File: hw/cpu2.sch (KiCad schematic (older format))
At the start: 0 parts

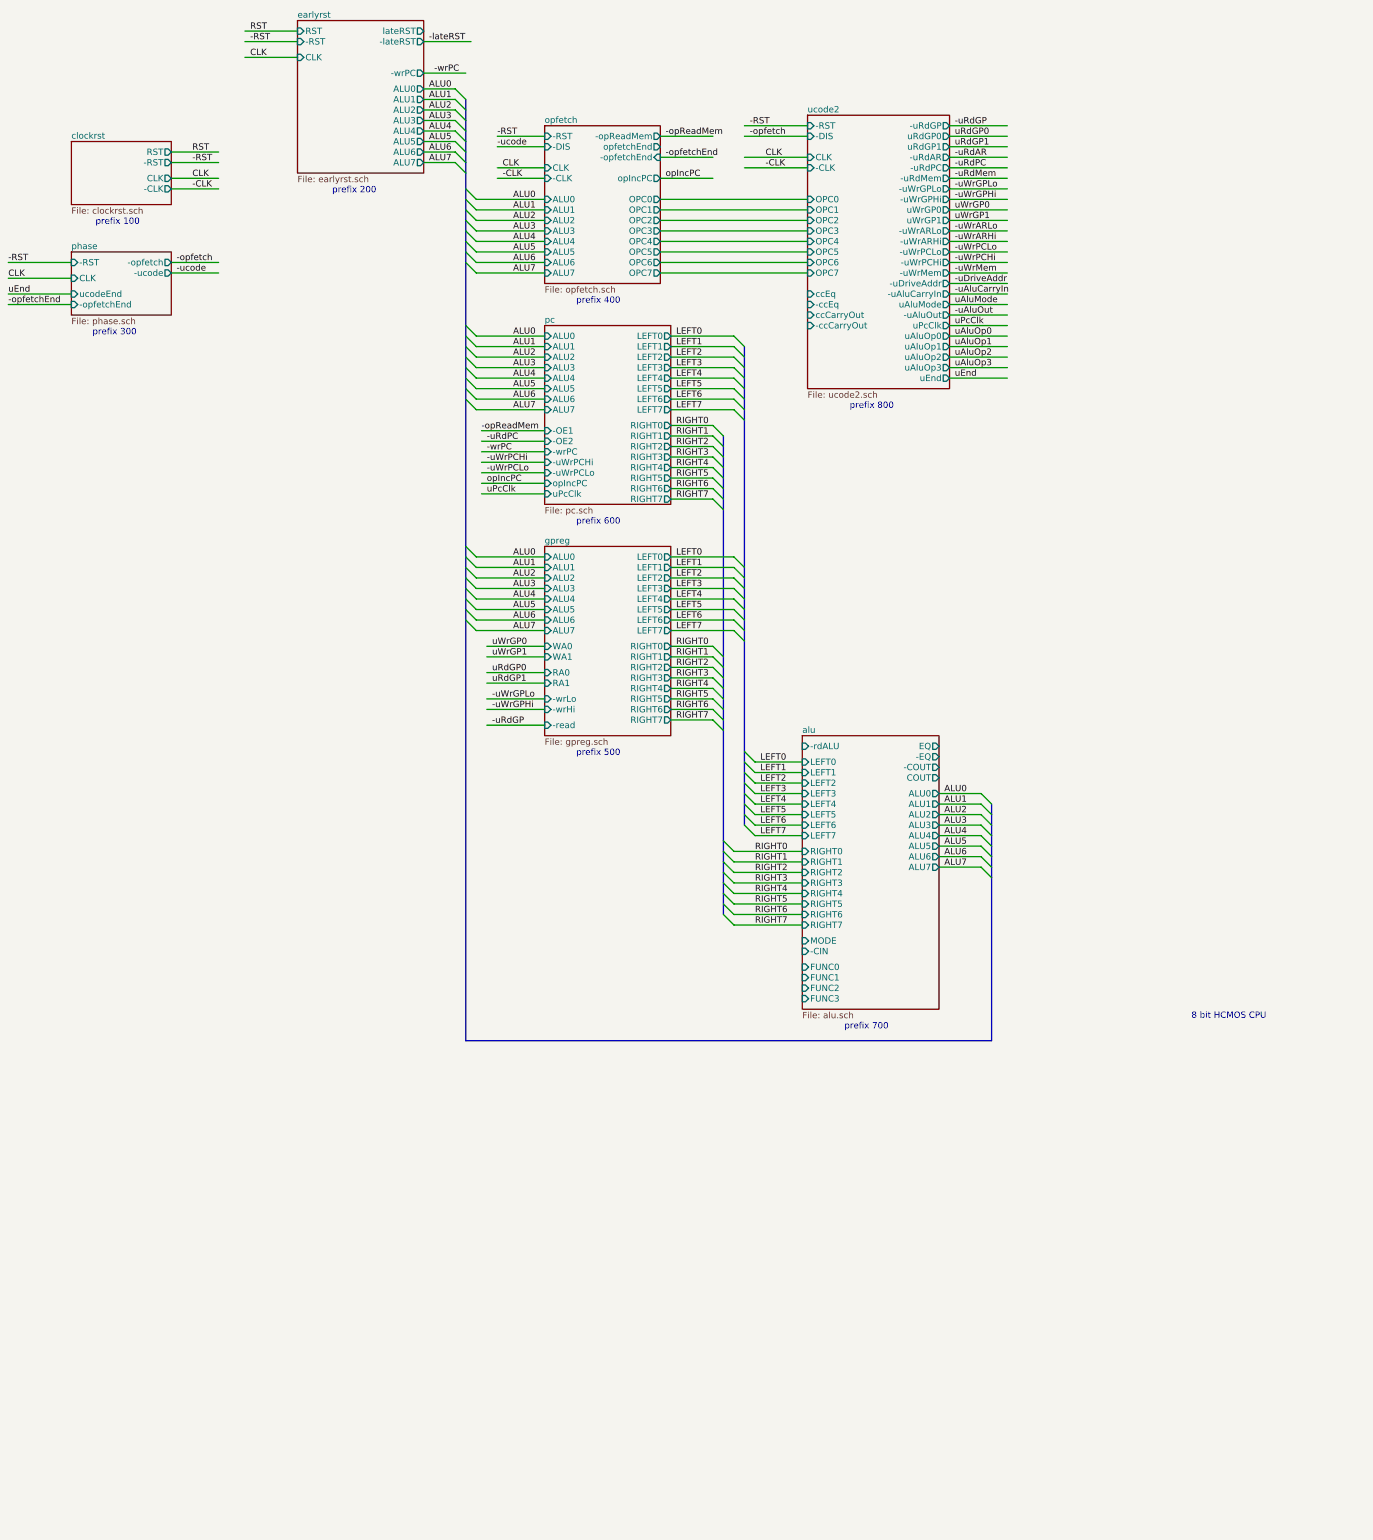
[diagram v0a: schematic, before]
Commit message: added bus/address register module
Used a '245 bus transceiver to do reads from
and writes to the external data bus, so the
control signals for reading and writing memory
changed (to -rwMem and memDir, rather than
separate read and write signals.)

At this point, I think all of the required modules
are in place, although not all of the connections are
shown on the top-level schematic.
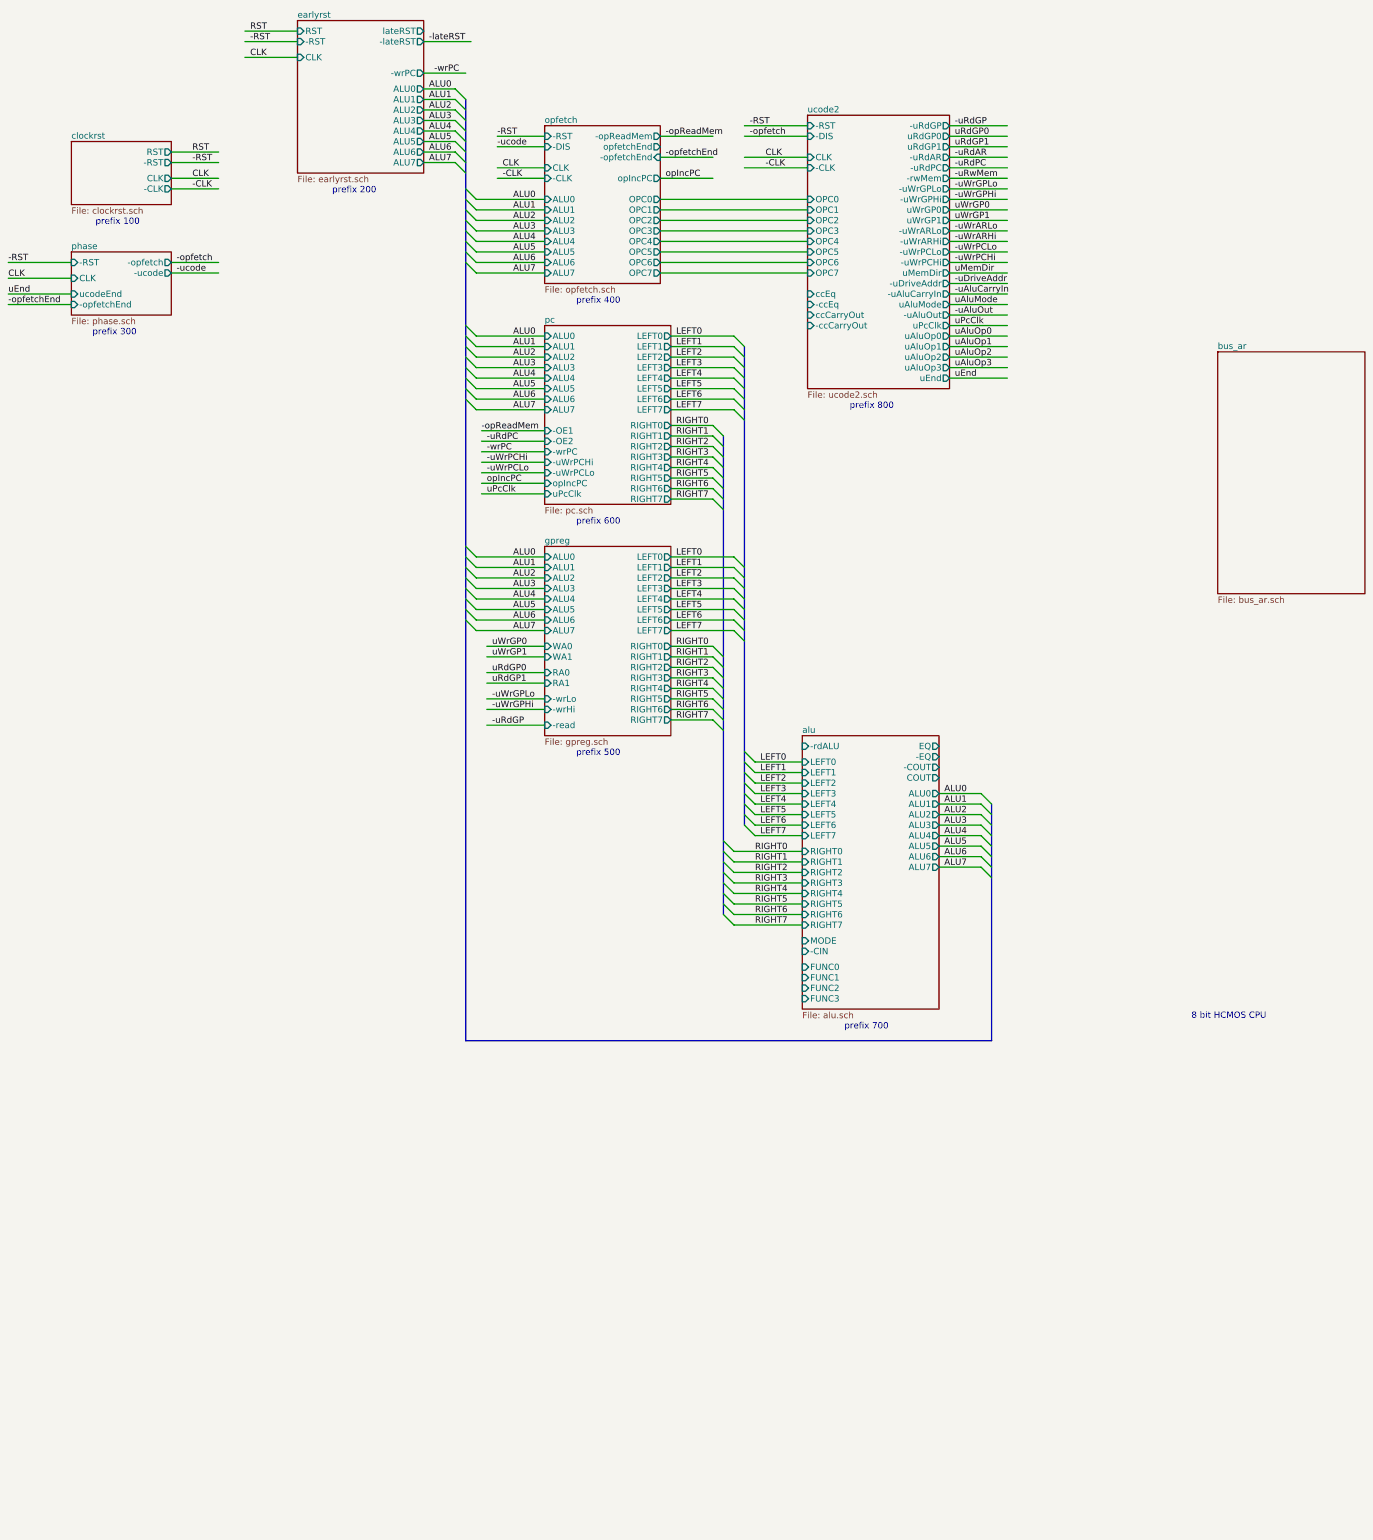
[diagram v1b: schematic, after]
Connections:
- net labels added: -uRwMem, uMemDir
- net labels removed: -uRdMem, -uWrMem
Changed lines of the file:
@@
 $Descr A3 16535 11693
 encoding utf-8
-Sheet 1 9
+Sheet 1 10
 Title ""
 Date ""
@@
 	4700 2050 5000 2050
 Wire Bus Line
-	5100 1450 5100 1550
-Wire Bus Line
-	5100 1550 5100 1650
-Wire Bus Line
-	5100 1650 5100 1750
-Wire Bus Line
-	5100 1750 5100 1850
-Wire Bus Line
-	5100 1850 5100 1950
-Wire Bus Line
-	5100 1950 5100 2050
-Wire Bus Line
-	5100 2050 5100 2150
-Wire Bus Line
-	5100 2150 5100 2300
-Wire Bus Line
-	5100 2300 5100 2400
-Wire Bus Line
-	5100 2400 5100 2500
-Wire Bus Line
-	5100 2500 5100 2600
-Wire Bus Line
-	5100 2600 5100 2700
-Wire Bus Line
-	5100 2700 5100 2800
-Wire Bus Line
-	5100 2800 5100 2900
-Wire Bus Line
-	5100 2900 5100 3000
-Wire Bus Line
-	5100 3000 5100 3600
-Wire Bus Line
-	5100 3600 5100 3700
-Wire Bus Line
-	5100 3700 5100 3800
-Wire Bus Line
-	5100 3800 5100 3900
-Wire Bus Line
-	5100 3900 5100 4000
-Wire Bus Line
-	5100 4000 5100 4100
-Wire Bus Line
-	5100 4100 5100 4200
-Wire Bus Line
-	5100 4200 5100 4300
-Wire Bus Line
-	5100 4300 5100 5700
-Wire Bus Line
-	5100 5700 5100 5800
-Wire Bus Line
-	5100 5800 5100 5900
-Wire Bus Line
-	5100 5900 5100 6000
-Wire Bus Line
-	5100 6000 5100 6100
-Wire Bus Line
-	5100 6100 5100 6200
-Wire Bus Line
-	5100 6200 5100 6300
-Wire Bus Line
-	5100 6300 5100 6400
-Wire Bus Line
-	5100 6400 5100 10400
+	5100 1450 5100 10400
 Wire Wire Line
 	5850 2400 5200 2400
@@
 	7050 4400 7650 4400
 Wire Bus Line
-	7750 3800 7750 3900
-Wire Bus Line
-	7750 3900 7750 4000
-Wire Bus Line
-	7750 4000 7750 4100
-Wire Bus Line
-	7750 4100 7750 4200
-Wire Bus Line
-	7750 4200 7750 4300
-Wire Bus Line
-	7750 4300 7750 4400
-Wire Bus Line
-	7750 4400 7750 4500
-Wire Bus Line
-	7750 4500 7750 5900
-Wire Bus Line
-	7750 5900 7750 6000
-Wire Bus Line
-	7750 6000 7750 6100
-Wire Bus Line
-	7750 6100 7750 6200
-Wire Bus Line
-	7750 6200 7750 6300
-Wire Bus Line
-	7750 6300 7750 6400
-Wire Bus Line
-	7750 6400 7750 6500
-Wire Bus Line
-	7750 6500 7750 6600
-Wire Bus Line
-	7750 6600 7750 7650
-Wire Bus Line
-	7750 7650 7750 7750
-Wire Bus Line
-	7750 7750 7750 7850
-Wire Bus Line
-	7750 7850 7750 7950
-Wire Bus Line
-	7750 7950 7750 8050
-Wire Bus Line
-	7750 8050 7750 8150
-Wire Bus Line
-	7750 8150 7750 8250
-Wire Bus Line
-	7750 8250 7750 8350
+	7750 3800 7750 8350
 Wire Wire Line
 	8300 7750 7850 7750
@@
 	7050 5250 7450 5250
 Wire Bus Line
-	7550 4650 7550 4750
-Wire Bus Line
-	7550 4750 7550 4850
-Wire Bus Line
-	7550 4850 7550 4950
-Wire Bus Line
-	7550 4950 7550 5050
-Wire Bus Line
-	7550 5050 7550 5150
-Wire Bus Line
-	7550 5150 7550 5250
-Wire Bus Line
-	7550 5250 7550 5350
-Wire Bus Line
-	7550 5350 7550 6750
-Wire Bus Line
-	7550 6750 7550 6850
-Wire Bus Line
-	7550 6850 7550 6950
-Wire Bus Line
-	7550 6950 7550 7050
-Wire Bus Line
-	7550 7050 7550 7150
-Wire Bus Line
-	7550 7150 7550 7250
-Wire Bus Line
-	7550 7250 7550 7350
-Wire Bus Line
-	7550 7350 7550 7450
-Wire Bus Line
-	7550 7450 7550 8500
-Wire Bus Line
-	7550 8500 7550 8600
-Wire Bus Line
-	7550 8600 7550 8700
-Wire Bus Line
-	7550 8700 7550 8800
-Wire Bus Line
-	7550 8800 7550 8900
-Wire Bus Line
-	7550 8900 7550 9000
-Wire Bus Line
-	7550 9000 7550 9100
-Wire Bus Line
-	7550 9100 7550 9200
+	7550 4650 7550 9200
 Wire Wire Line
 	8300 8600 7650 8600
@@
 	8300 9300 7650 9300
 Wire Bus Line
-	10100 10400 5100 10400
+	5100 10400 10100 10400
 Wire Bus Line
-	10100 8150 10100 8250
-Wire Bus Line
-	10100 8250 10100 8350
-Wire Bus Line
-	10100 8350 10100 8450
-Wire Bus Line
-	10100 8450 10100 8550
-Wire Bus Line
-	10100 8550 10100 8650
-Wire Bus Line
-	10100 8650 10100 8750
-Wire Bus Line
-	10100 8750 10100 8850
-Wire Bus Line
-	10100 8850 10100 10400
+	10100 10400 10100 8150
 Wire Wire Line
 	9600 8050 10000 8050
@@
 F17 "-uRdAR" O R 9700 2000 60
 F18 "-uRdPC" O R 9700 2100 60
-F19 "-uRdMem" O R 9700 2200 60
-F20 "-uWrGPLo" O R 9700 2300 60
-F21 "-uWrGPHi" O R 9700 2400 60
-F22 "uWrGP0" O R 9700 2500 60
-F23 "uWrGP1" O R 9700 2600 60
-F24 "-uWrARLo" O R 9700 2700 60
-F25 "-uWrARHi" O R 9700 2800 60
-F26 "-uWrPCLo" O R 9700 2900 60
-F27 "-uWrPCHi" O R 9700 3000 60
-F28 "-uWrMem" O R 9700 3100 60
-F29 "-uAluCarryIn" O R 9700 3300 60
-F30 "uAluMode" O R 9700 3400 60
-F31 "uAluOp0" O R 9700 3700 60
-F32 "uAluOp1" O R 9700 3800 60
-F33 "uAluOp2" O R 9700 3900 60
-F34 "uAluOp3" O R 9700 4000 60
-F35 "-uAluOut" O R 9700 3500 60
-F36 "ccEq" I L 8350 3300 60
-F37 "-ccEq" I L 8350 3400 60
-F38 "ccCarryOut" I L 8350 3500 60
-F39 "-ccCarryOut" I L 8350 3600 60
-F40 "-uDriveAddr" O R 9700 3200 60
-F41 "uPcClk" O R 9700 3600 60
-F42 "uEnd" O R 9700 4100 60
+F19 "-uWrGPLo" O R 9700 2300 60
+F20 "-uWrGPHi" O R 9700 2400 60
+F21 "uWrGP0" O R 9700 2500 60
+F22 "uWrGP1" O R 9700 2600 60
+F23 "-uWrARLo" O R 9700 2700 60
+F24 "-uWrARHi" O R 9700 2800 60
+F25 "-uWrPCLo" O R 9700 2900 60
+F26 "-uWrPCHi" O R 9700 3000 60
+F27 "-uAluCarryIn" O R 9700 3300 60
+F28 "uAluMode" O R 9700 3400 60
+F29 "uAluOp0" O R 9700 3700 60
+F30 "uAluOp1" O R 9700 3800 60
+F31 "uAluOp2" O R 9700 3900 60
+F32 "uAluOp3" O R 9700 4000 60
+F33 "-uAluOut" O R 9700 3500 60
+F34 "ccEq" I L 8350 3300 60
+F35 "-ccEq" I L 8350 3400 60
+F36 "ccCarryOut" I L 8350 3500 60
+F37 "-ccCarryOut" I L 8350 3600 60
+F38 "-uDriveAddr" O R 9700 3200 60
+F39 "uPcClk" O R 9700 3600 60
+F40 "uEnd" O R 9700 4100 60
+F41 "-rwMem" O R 9700 2200 60
+F42 "uMemDir" O R 9700 3100 60
 $EndSheet
 Wire Wire Line
@@
 	9700 2100 10250 2100
 Wire Wire Line
-	9700 2200 10250 2200
-Wire Wire Line
 	9700 2300 10250 2300
 Wire Wire Line
@@
 Wire Wire Line
 	9700 3000 10250 3000
-Wire Wire Line
-	9700 3100 10250 3100
 Wire Wire Line
 	9700 3200 10250 3200
@@
 Text Label 9750 2100 0    60   ~ 0
 -uRdPC
-Text Label 9750 2200 0    60   ~ 0
--uRdMem
 Text Label 9750 2300 0    60   ~ 0
 -uWrGPLo
@@
 Text Label 9750 3000 0    60   ~ 0
 -uWrPCHi
-Text Label 9750 3100 0    60   ~ 0
--uWrMem
 Text Label 9750 3200 0    60   ~ 0
 -uDriveAddr
@@
 Text Label 5350 7400 0    60   ~ 0
 -uRdGP
+$Sheet
+S 12250 3850 1400 2300
+U 595E8C5F
+F0 "bus_ar" 60
+F1 "bus_ar.sch" 60
+$EndSheet
+Wire Wire Line
+	9700 2200 10250 2200
+Text Label 9750 2200 0    60   ~ 0
+-uRwMem
+Wire Wire Line
+	9700 3100 10250 3100
+Text Label 9750 3100 0    60   ~ 0
+uMemDir
 $EndSCHEMATC

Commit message: finish connections on top-level schematic
A lot of careful inspection is necessary, but at this
point all of the hardware components should be in place
(unless I am totally missing something.)
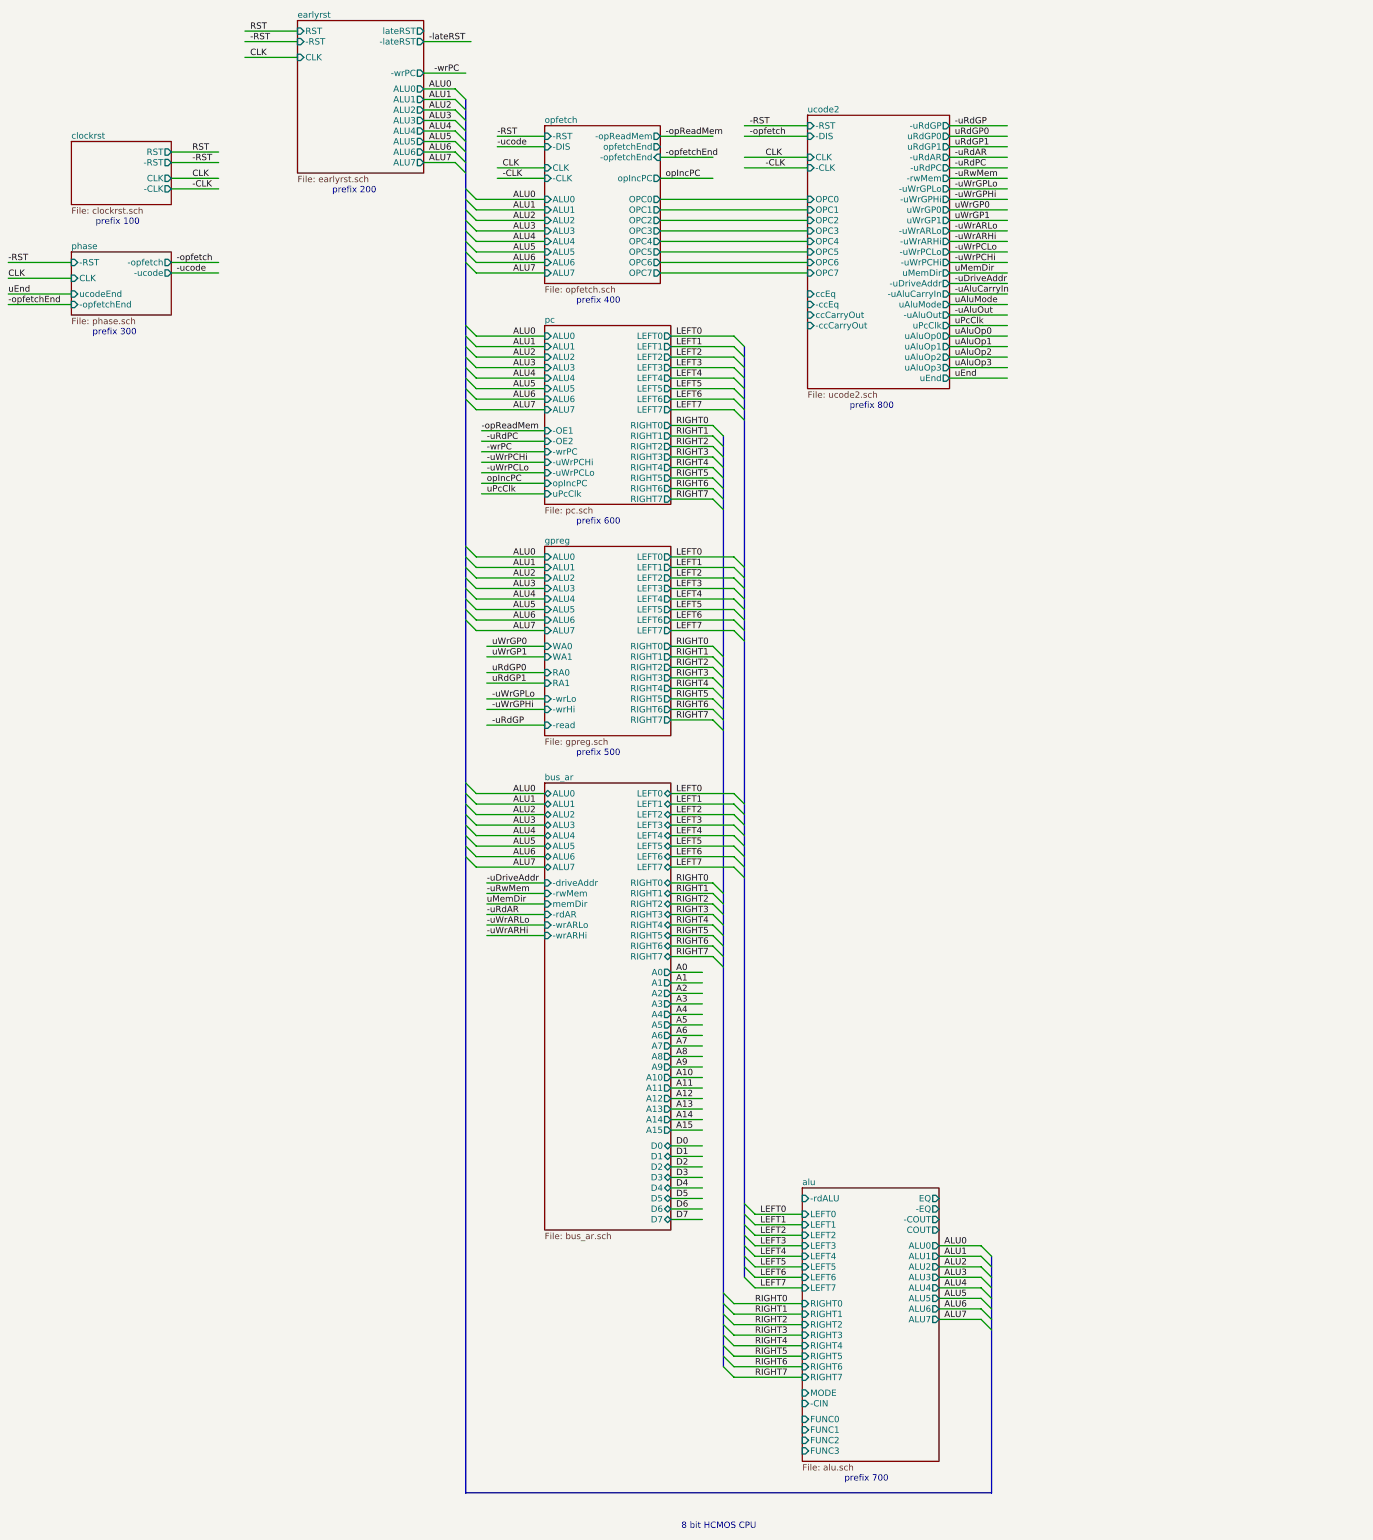
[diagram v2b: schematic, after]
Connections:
- net labels added: A0, A1, A10, A11, A12, A13, A14, A15, A2, A3, A4, A5, A6, A7, A8, A9, D0, D1, D2, D3, D4, D5, D6, D7
- wire segments 161 -> 215

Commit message: connect condition code signals to ucode module
These are needed by the conditional branch logic.
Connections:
- net labels added: -COUT, -EQ, COUT, EQ
- wire segments 215 -> 223
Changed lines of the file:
@@
 Text Label 7100 12100 0    60   ~ 0
 D7
+Wire Wire Line
+	9600 11900 10000 11900
+Wire Wire Line
+	9600 12000 10000 12000
+Wire Wire Line
+	9600 12100 10000 12100
+Wire Wire Line
+	9600 12200 10000 12200
+Text Label 9650 11900 0    60   ~ 0
+EQ
+Text Label 9650 12000 0    60   ~ 0
+-EQ
+Text Label 9650 12100 0    60   ~ 0
+-COUT
+Text Label 9650 12200 0    60   ~ 0
+COUT
+Wire Wire Line
+	8350 3300 7900 3300
+Wire Wire Line
+	8350 3400 7900 3400
+Wire Wire Line
+	8350 3500 7900 3500
+Wire Wire Line
+	8350 3600 7900 3600
+Text Label 7950 3300 0    60   ~ 0
+EQ
+Text Label 7950 3400 0    60   ~ 0
+-EQ
+Text Label 7950 3500 0    60   ~ 0
+COUT
+Text Label 7950 3600 0    60   ~ 0
+-COUT
 $EndSCHEMATC
